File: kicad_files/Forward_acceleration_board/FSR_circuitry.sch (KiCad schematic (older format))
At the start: 49 parts

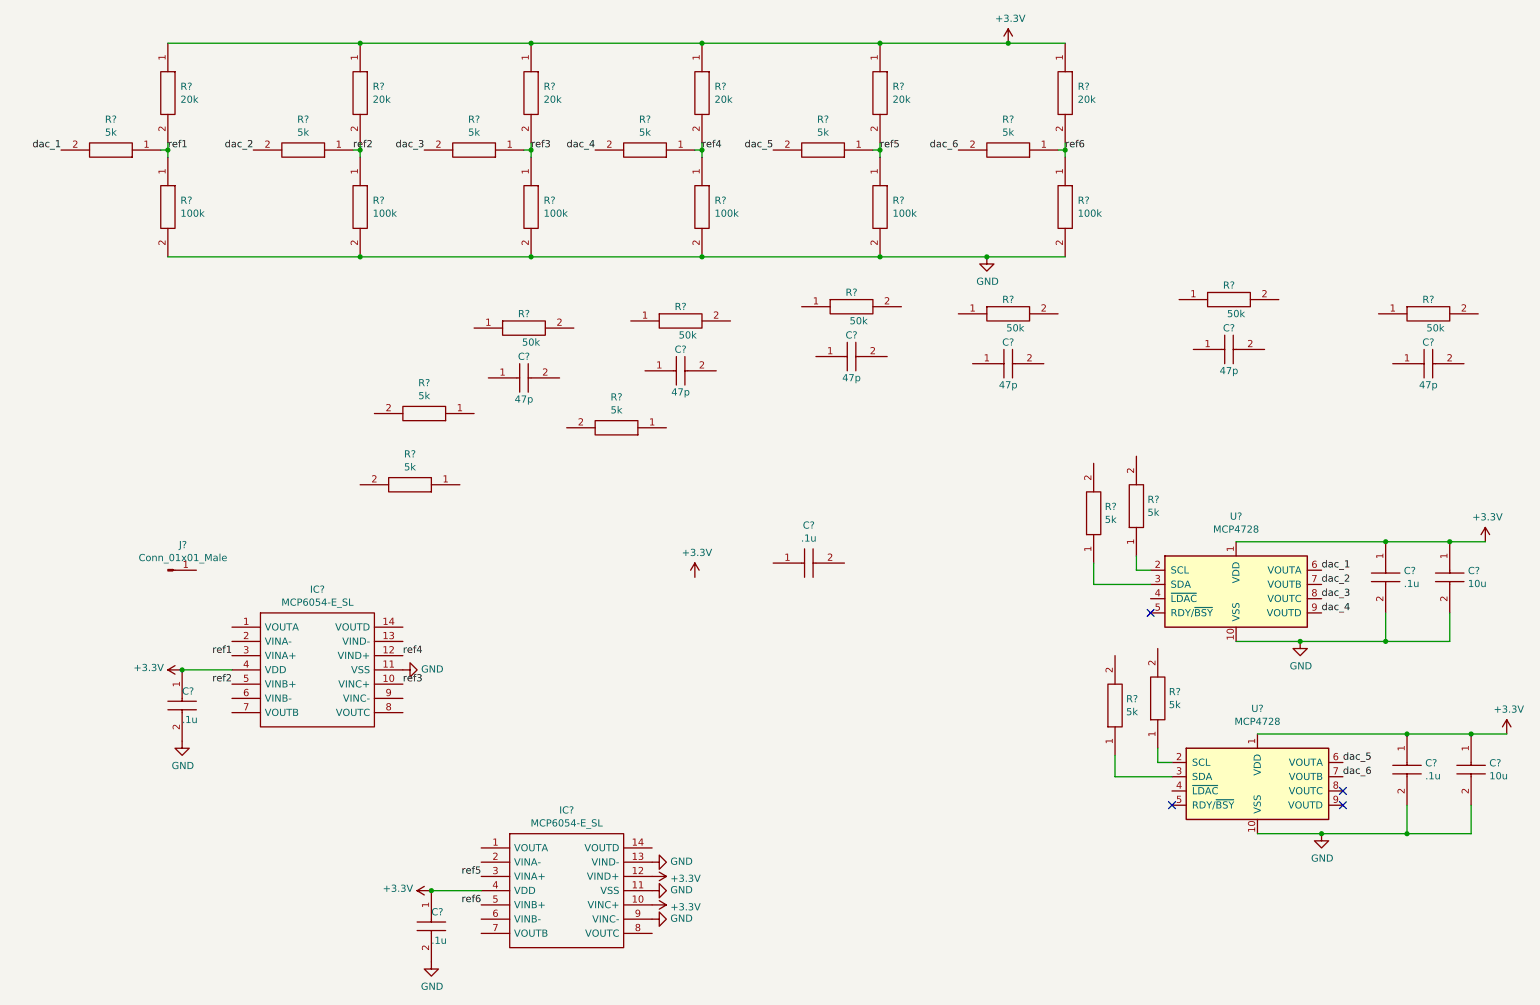
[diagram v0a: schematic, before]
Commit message: reogranized file locations, improved DSC controller pcb with edged margin on edges and rounded corners.  Completed Acceleration control board schematic
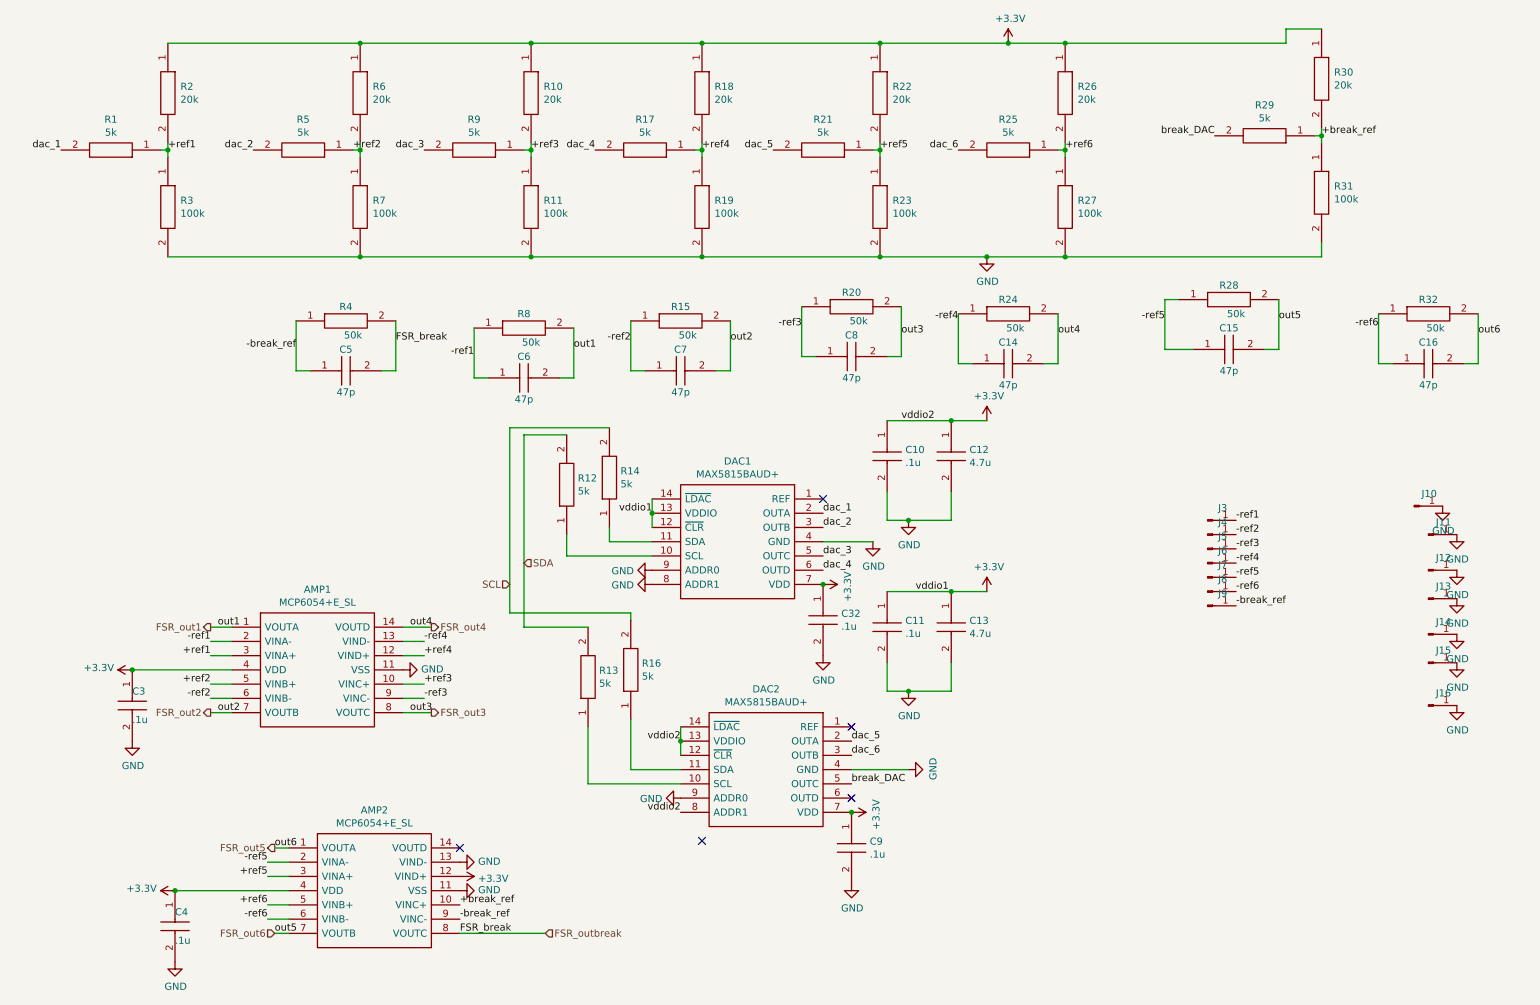
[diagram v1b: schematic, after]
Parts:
- removed C? (x2): .1u, CAPC2012X145N, symbol AS0805KKX7R0BB104:AS0805KKX7R0BB104
- removed C? (x2): 10u, CAPC1005X55N, symbol GRM155C80G106ME44D:GRM155C80G106ME44D
- removed J?: Conn_01x01_Male, symbol Connector:Conn_01x01_Male
- removed R? (x3): 5k, RESC1608X55N, symbol MCT0603PD4991DP500:MCT0603PD4991DP500
- removed U? (x2): MCP4728, Package_SO:MSOP-10_3x3mm_P0.5mm, symbol Analog_DAC:MCP4728
- added C10, C32, C9: .1u, AS0805KKX7R0BB104:CAPC2012X145N, symbol AS0805KKX7R0BB104:AS0805KKX7R0BB104
- added C12, C13: 4.7u, CGA6M3X7S2A475K200AB:CAPC3225X200N, symbol CGA6M3X7S2A475K200AB:CGA6M3X7S2A475K200AB
- added C5: 47p, GRM155C91C105ME11J:CAPC1005X55N, symbol GRM1555C1H470FA01J:GRM1555C1H470FA01J
- added DAC1, DAC2: MAX5815BAUD+, MAX5815BAUD+:SOP65P640X110-14N, symbol MAX5815BAUD+:MAX5815BAUD+
- added J10, J11, J12, J13, J14, J15, J16, J3, J4, J5, J6, J7, J8, J9: Conn_01x01_Male, symbol Connector:Conn_01x01_Male
- added R29: 5k, ERJ3RQF4R7V:RESC1608X55N, symbol MCT0603PD4991DP500:MCT0603PD4991DP500
- added R30: 20k, ERJ3RQF4R7V:RESC1608X55N, symbol MCT0603PD2002DP500:MCT0603PD2002DP500
- added R31: 100k, ERJ3RQF4R7V:RESC1608X55N, symbol MCT0603PD1003DP500:MCT0603PD1003DP500
- added R4: 50k, ERJ3RQF4R7V:RESC1608X55N, symbol MCT0603PD4992DP500:MCT0603PD4992DP500
- AMP1, AMP2: renamed from IC?; value MCP6054-E_SL -> MCP6054+E_SL; footprint SOIC127P600X175-14N -> MCP6054-E_SL:SOIC127P600X175-14N
- C11, C3, C4: renamed from C?; footprint CAPC2012X145N -> AS0805KKX7R0BB104:CAPC2012X145N
- C14, C15, C16, C6, C7, C8: renamed from C?; footprint CAPC1005X55N -> GRM155C91C105ME11J:CAPC1005X55N
- R1, R10, R11, R12, R13, R14, R15, R16, R17, R18, R19, R2, R20, R21, R22, R23, R24, R25, R26, R27, R28, R3, R32, R5, R6, R7, R8, R9: renamed from R?; footprint RESC1608X55N -> ERJ3RQF4R7V:RESC1608X55N
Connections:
- net +3V3: now also C10.1, C12.1, C13.1, C32.1, C9.1, DAC1.12 (~CLR), DAC1.13 (VDDIO), DAC1.14 (~LDAC), DAC1.7 (VDD), DAC2.12 (~CLR), DAC2.13 (VDDIO), DAC2.14 (~LDAC), DAC2.7 (VDD), DAC2.8 (ADDR1), R30.1; no longer AMP2.10 (VINC+)
- net GND: now also C10.2, C12.2, C13.2, C32.2, C9.2, DAC1.4 (GND), DAC1.8 (ADDR1), DAC1.9 (ADDR0), DAC2.4 (GND), DAC2.9 (ADDR0), J10.1 (Pin_1), J11.1 (Pin_1), J12.1 (Pin_1), J13.1 (Pin_1), J14.1 (Pin_1), J15.1 (Pin_1), J16.1 (Pin_1), R31.2; no longer AMP2.9 (VINC-)
- net dac_1: now also DAC1.2 (OUTA)
- net dac_2: now also DAC1.3 (OUTB)
- net dac_3: now also DAC1.5 (OUTC)
- net dac_4: now also DAC1.6 (OUTD)
- net dac_5: now also DAC2.2 (OUTA)
- net dac_6: now also DAC2.3 (OUTB)
- net -ref1: now reaches R8.1
- net -ref1: now also AMP1.2 (VINA-), C6.1, J3.1 (Pin_1)
- net FSR_out1: now reaches R8.2
- net FSR_out1: now also AMP1.1 (VOUTA), C6.2
- net at R16.1: now also DAC2.11 (SDA)
- net at R13.1: now also DAC2.10 (SCL)
- net FSR_out5: now reaches AMP2.1 (VOUTA)
- net FSR_out5: now also C16.2, R32.2
- net -ref5: now reaches AMP2.2 (VINA-)
- net -ref5: now also C15.1, R28.1, J7.1 (Pin_1)
- net -ref6: now reaches AMP2.6 (VINB-)
- net -ref6: now also C16.1, R32.1, J8.1 (Pin_1)
- net FSR_out6: now reaches AMP2.7 (VOUTB)
- net FSR_out6: now also C15.2, R28.2
- net FSR_outbreak: now reaches AMP2.8 (VOUTC)
- net FSR_outbreak: now also C5.2, R4.2
- net -ref4: now reaches AMP1.13 (VIND-)
- net -ref4: now also C14.1, R24.1, J6.1 (Pin_1)
- net FSR_out4: now reaches AMP1.14 (VOUTD)
- net FSR_out4: now also C14.2, R24.2
- net -ref2: now reaches AMP1.6 (VINB-)
- net -ref2: now also C7.1, R15.1, J4.1 (Pin_1)
- net FSR_out2: now reaches AMP1.7 (VOUTB)
- net FSR_out2: now also C7.2, R15.2
- net FSR_out3: now reaches AMP1.8 (VOUTC)
- net FSR_out3: now also C8.2, R20.2
- net -ref3: now reaches AMP1.9 (VINC-)
- net -ref3: now also C8.1, R20.1, J5.1 (Pin_1)
- net SDA: now reaches R13.2
- net SDA: now also R12.2
- net SCL: now reaches R16.2
- net SCL: now also R14.2
- net at R14.1: now also DAC1.11 (SDA)
- net at R12.1: now also DAC1.10 (SCL)
- net ref1 renamed +ref1
- net ref2 renamed +ref2
- net ref3 renamed +ref3
- net ref4 renamed +ref4
- net ref5 renamed +ref5
- net ref6 renamed +ref6
- new net +break_ref: AMP2.10 (VINC+), R29.1, R30.2, R31.1
- new net -break_ref: AMP2.9 (VINC-), C5.1, J9.1 (Pin_1), R4.1
- new net break_DAC: DAC2.5 (OUTC), R29.2
- no-connect marks 4 -> 5
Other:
- moved on the sheet: AMP2, C11, C3, C4, R12, R13, R14, R16

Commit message: nearly completed forward acceleration control board rounded edges and established clearence for motor control board made progress canabalizing Vedder's code for motor control
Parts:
- J10, J11, J12, J13, J14, J15, J16, J3, J4, J5, J6, J7, J8, J9: footprint (none) -> Wire_Pads:SolderWirePad_1x01_SMD_1.27x2.54mm
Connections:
- net +3V3: now also AMP1.12 (VIND+), R29.2; no longer AMP2.12 (VIND+), R30.1
- net +break_ref: now also R17.2, R18.2, R19.1; no longer R29.1, R30.2, R31.1
- net +ref1: now also R1.2; no longer R1.1
- net +ref2: now also R5.2; no longer R5.1
- net +ref3: now also R9.2; no longer R9.1
- net +ref4: now also AMP2.12 (VIND+), R29.1, R30.1, R31.1; no longer AMP1.12 (VIND+), R17.1, R18.2, R19.1
- net +ref5: now also R21.2; no longer R21.1
- net +ref6: now also R25.2; no longer R25.1
- net -break_ref: now also C14.1, R24.1; no longer C5.1, R4.1
- net -ref4: now also AMP2.13 (VIND-), C5.1, R4.1; no longer AMP1.13 (VIND-), C14.1, R24.1
- net FSR_out4: now also AMP2.14 (VOUTD), C5.2, R4.2; no longer AMP1.14 (VOUTD), C14.2, R24.2
- net FSR_out5: now also C15.2, R28.2; no longer C16.2, R32.2
- net FSR_out6: now also C16.2, R32.2; no longer C15.2, R28.2
- net FSR_outbreak: now also C14.2, R24.2; no longer C5.2, R4.2
- net GND: now also AMP1.13 (VIND-); no longer AMP2.13 (VIND-)
- net break_DAC: now also R17.1; no longer R29.2
- net dac_1: now also R1.1; no longer R1.2
- net dac_2: now also R5.1; no longer R5.2
- net dac_3: now also R9.1; no longer R9.2
- net dac_4: now also DAC2.6 (OUTD), R30.2; no longer DAC1.6 (OUTD), R17.2
- net dac_5: now also R21.1; no longer R21.2
- net dac_6: now also R25.1; no longer R25.2
- no-connect marks 5 -> 4
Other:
- moved on the sheet: C14, R17, R18, R19, R21, R22, R23, R24, R25, R26, R27, R29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

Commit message: updated BOMS for boards and added battery pack wiring schematic
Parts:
- J10, J11, J12, J13, J14, J15, J16, J3, J4, J5, J6, J7, J8, J9: symbol Connector:Conn_01x01_Male -> Forward_acceleration_board-rescue:Conn_01x01_Male-Connector
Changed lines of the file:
@@
 $EndComp
 $Comp
-L power:GND #PWR0105
+L Forward_acceleration_board-rescue:GND-power #PWR0105
 U 1 1 5D8E34E0
 P 3200 5200
@@
 Connection ~ 4100 800
 $Comp
-L power:+3.3V #PWR0107
+L Forward_acceleration_board-rescue:+3.3V-power #PWR0107
 U 1 1 5D8E6EA9
 P 7450 800
@@
 Connection ~ 4100 2300
 $Comp
-L power:GND #PWR0108
+L Forward_acceleration_board-rescue:GND-power #PWR0108
 U 1 1 5D8EB31F
 P 7300 2300
@@
 $EndComp
 $Comp
-L power:+3.3V #PWR0109
+L Forward_acceleration_board-rescue:+3.3V-power #PWR0109
 U 1 1 5D8E337A
 P 1600 6750
@@
 Connection ~ 1600 6750
 $Comp
-L power:GND #PWR0110
+L Forward_acceleration_board-rescue:GND-power #PWR0110
 U 1 1 5D8F17E9
 P 1600 7250
@@
 $EndComp
 $Comp
-L power:+3.3V #PWR0111
+L Forward_acceleration_board-rescue:+3.3V-power #PWR0111
 U 1 1 5D8F1D89
 P 1300 5200
@@
 	2000 5200 1300 5200
 $Comp
-L power:GND #PWR0112
+L Forward_acceleration_board-rescue:GND-power #PWR0112
 U 1 1 5D8F1D91
 P 1300 5700
@@
 $EndComp
 $Comp
-L power:+3.3V #PWR0113
+L Forward_acceleration_board-rescue:+3.3V-power #PWR0113
 U 1 1 5D908625
 P 7300 4650
@@
 	6600 5150 6600 5350
 $Comp
-L power:GND #PWR0114
+L Forward_acceleration_board-rescue:GND-power #PWR0114
 U 1 1 5D908644
 P 6500 4300
@@
 break_DAC
 $Comp
-L Connector:Conn_01x01_Male J3
+L Forward_acceleration_board-rescue:Conn_01x01_Male-Connector J3
 U 1 1 5D9E5847
 P 8850 4150
+AR Path="/5D9E5847" Ref="J3"  Part="1"
+AR Path="/5D8CBEA0/5D9E5847" Ref="J3"  Part="1"
 F 0 "J3" H 8956 4237 50  0000 C CNN
 F 1 "Conn_01x01_Male" H 8956 4237 50  0001 C CNN
@@
 $EndComp
 $Comp
-L Connector:Conn_01x01_Male J4
+L Forward_acceleration_board-rescue:Conn_01x01_Male-Connector J4
 U 1 1 5D9E58E5
 P 8850 4250
+AR Path="/5D9E58E5" Ref="J4"  Part="1"
+AR Path="/5D8CBEA0/5D9E58E5" Ref="J4"  Part="1"
 F 0 "J4" H 8956 4337 50  0000 C CNN
 F 1 "Conn_01x01_Male" H 8956 4337 50  0001 C CNN
@@
 $EndComp
 $Comp
-L Connector:Conn_01x01_Male J6
+L Forward_acceleration_board-rescue:Conn_01x01_Male-Connector J6
 U 1 1 5D9E59AA
 P 8850 4450
+AR Path="/5D9E59AA" Ref="J6"  Part="1"
+AR Path="/5D8CBEA0/5D9E59AA" Ref="J6"  Part="1"
 F 0 "J6" H 8956 4537 50  0000 C CNN
 F 1 "Conn_01x01_Male" H 8956 4537 50  0001 C CNN
@@
 $EndComp
 $Comp
-L Connector:Conn_01x01_Male J5
+L Forward_acceleration_board-rescue:Conn_01x01_Male-Connector J5
 U 1 1 5D9E5A72
 P 8850 4350
+AR Path="/5D9E5A72" Ref="J5"  Part="1"
+AR Path="/5D8CBEA0/5D9E5A72" Ref="J5"  Part="1"
 F 0 "J5" H 8956 4437 50  0000 C CNN
 F 1 "Conn_01x01_Male" H 8956 4437 50  0001 C CNN
@@
 $EndComp
 $Comp
-L Connector:Conn_01x01_Male J7
+L Forward_acceleration_board-rescue:Conn_01x01_Male-Connector J7
 U 1 1 5D9E5CB8
 P 8850 4550
+AR Path="/5D9E5CB8" Ref="J7"  Part="1"
+AR Path="/5D8CBEA0/5D9E5CB8" Ref="J7"  Part="1"
 F 0 "J7" H 8956 4637 50  0000 C CNN
 F 1 "Conn_01x01_Male" H 8956 4637 50  0001 C CNN
@@
 $EndComp
 $Comp
-L Connector:Conn_01x01_Male J8
+L Forward_acceleration_board-rescue:Conn_01x01_Male-Connector J8
 U 1 1 5D9E5D3A
 P 8850 4650
+AR Path="/5D9E5D3A" Ref="J8"  Part="1"
+AR Path="/5D8CBEA0/5D9E5D3A" Ref="J8"  Part="1"
 F 0 "J8" H 8956 4737 50  0000 C CNN
 F 1 "Conn_01x01_Male" H 8956 4737 50  0001 C CNN
@@
 $EndComp
 $Comp
-L Connector:Conn_01x01_Male J9
+L Forward_acceleration_board-rescue:Conn_01x01_Male-Connector J9
 U 1 1 5D9E5DC8
 P 8850 4750
+AR Path="/5D9E5DC8" Ref="J9"  Part="1"
+AR Path="/5D8CBEA0/5D9E5DC8" Ref="J9"  Part="1"
 F 0 "J9" H 8956 4837 50  0000 C CNN
 F 1 "Conn_01x01_Male" H 8956 4837 50  0001 C CNN
@@
 $EndComp
 $Comp
-L Connector:Conn_01x01_Male J10
+L Forward_acceleration_board-rescue:Conn_01x01_Male-Connector J10
 U 1 1 5D9E5F6F
 P 10300 4050
+AR Path="/5D9E5F6F" Ref="J10"  Part="1"
+AR Path="/5D8CBEA0/5D9E5F6F" Ref="J10"  Part="1"
 F 0 "J10" H 10406 4137 50  0000 C CNN
 F 1 "Conn_01x01_Male" H 10406 4137 50  0001 C CNN
@@
 $EndComp
 $Comp
-L Connector:Conn_01x01_Male J11
+L Forward_acceleration_board-rescue:Conn_01x01_Male-Connector J11
 U 1 1 5D9E5F76
 P 10400 4250
+AR Path="/5D9E5F76" Ref="J11"  Part="1"
+AR Path="/5D8CBEA0/5D9E5F76" Ref="J11"  Part="1"
 F 0 "J11" H 10506 4337 50  0000 C CNN
 F 1 "Conn_01x01_Male" H 10506 4337 50  0001 C CNN
@@
 $EndComp
 $Comp
-L Connector:Conn_01x01_Male J12
+L Forward_acceleration_board-rescue:Conn_01x01_Male-Connector J12
 U 1 1 5D9E5F7D
 P 10400 4500
+AR Path="/5D9E5F7D" Ref="J12"  Part="1"
+AR Path="/5D8CBEA0/5D9E5F7D" Ref="J12"  Part="1"
 F 0 "J12" H 10506 4587 50  0000 C CNN
 F 1 "Conn_01x01_Male" H 10506 4587 50  0001 C CNN
@@
 $EndComp
 $Comp
-L Connector:Conn_01x01_Male J13
+L Forward_acceleration_board-rescue:Conn_01x01_Male-Connector J13
 U 1 1 5D9E5F84
 P 10400 4700
+AR Path="/5D9E5F84" Ref="J13"  Part="1"
+AR Path="/5D8CBEA0/5D9E5F84" Ref="J13"  Part="1"
 F 0 "J13" H 10506 4787 50  0000 C CNN
 F 1 "Conn_01x01_Male" H 10506 4787 50  0001 C CNN
@@
 $EndComp
 $Comp
-L Connector:Conn_01x01_Male J14
+L Forward_acceleration_board-rescue:Conn_01x01_Male-Connector J14
 U 1 1 5D9E5F8B
 P 10400 4950
+AR Path="/5D9E5F8B" Ref="J14"  Part="1"
+AR Path="/5D8CBEA0/5D9E5F8B" Ref="J14"  Part="1"
 F 0 "J14" H 10506 5037 50  0000 C CNN
 F 1 "Conn_01x01_Male" H 10506 5037 50  0001 C CNN
@@
 $EndComp
 $Comp
-L Connector:Conn_01x01_Male J15
+L Forward_acceleration_board-rescue:Conn_01x01_Male-Connector J15
 U 1 1 5D9E5F92
 P 10400 5150
+AR Path="/5D9E5F92" Ref="J15"  Part="1"
+AR Path="/5D8CBEA0/5D9E5F92" Ref="J15"  Part="1"
 F 0 "J15" H 10506 5237 50  0000 C CNN
 F 1 "Conn_01x01_Male" H 10506 5237 50  0001 C CNN
@@
 $EndComp
 $Comp
-L Connector:Conn_01x01_Male J16
+L Forward_acceleration_board-rescue:Conn_01x01_Male-Connector J16
 U 1 1 5D9E5F99
 P 10400 5450
+AR Path="/5D9E5F99" Ref="J16"  Part="1"
+AR Path="/5D8CBEA0/5D9E5F99" Ref="J16"  Part="1"
 F 0 "J16" H 10506 5537 50  0000 C CNN
 F 1 "Conn_01x01_Male" H 10506 5537 50  0001 C CNN
@@
 $EndComp
 $Comp
-L power:GND #PWR0117
+L Forward_acceleration_board-rescue:GND-power #PWR0117
 U 1 1 5D9EA9F2
 P 10600 4950
@@
 $EndComp
 $Comp
-L power:GND #PWR0118
+L Forward_acceleration_board-rescue:GND-power #PWR0118
 U 1 1 5D9EAFE2
 P 10500 4050
@@
 $EndComp
 $Comp
-L power:GND #PWR0119
+L Forward_acceleration_board-rescue:GND-power #PWR0119
 U 1 1 5D9EB06B
 P 10600 4250
@@
 $EndComp
 $Comp
-L power:GND #PWR0120
+L Forward_acceleration_board-rescue:GND-power #PWR0120
 U 1 1 5D9EB133
 P 10600 4500
@@
 $EndComp
 $Comp
-L power:GND #PWR0121
+L Forward_acceleration_board-rescue:GND-power #PWR0121
 U 1 1 5D9EB3BE
 P 10600 4700
@@
 $EndComp
 $Comp
-L power:GND #PWR0122
+L Forward_acceleration_board-rescue:GND-power #PWR0122
 U 1 1 5D9EBD62
 P 10600 5150
@@
 $EndComp
 $Comp
-L power:GND #PWR0125
+L Forward_acceleration_board-rescue:GND-power #PWR0125
 U 1 1 5D9EBEB2
 P 10600 5450
@@
 	6600 5350 6750 5350
 $Comp
-L power:GND #PWR0126
+L Forward_acceleration_board-rescue:GND-power #PWR0126
 U 1 1 5DA2AB93
 P 6750 5350
@@
 	6750 5350 7050 5350
 $Comp
-L power:+3.3V #PWR0127
+L Forward_acceleration_board-rescue:+3.3V-power #PWR0127
 U 1 1 5DA3C029
 P 7300 3450
@@
 	6600 4150 6750 4150
 $Comp
-L power:GND #PWR0128
+L Forward_acceleration_board-rescue:GND-power #PWR0128
 U 1 1 5DA3C051
 P 6750 4150
@@
 	6750 4150 7050 4150
 $Comp
-L power:GND #PWR0129
+L Forward_acceleration_board-rescue:GND-power #PWR0129
 U 1 1 5DA4BB6C
 P 5150 6100
@@
 vddio2
 $Comp
-L power:GND #PWR0130
+L Forward_acceleration_board-rescue:GND-power #PWR0130
 U 1 1 5DA6DB6A
 P 4950 4500
@@
 $EndComp
 $Comp
-L power:GND #PWR0131
+L Forward_acceleration_board-rescue:GND-power #PWR0131
 U 1 1 5DA6DC32
 P 4950 4600
@@
 Connection ~ 4950 4100
 $Comp
-L power:+3.3V #PWR0132
+L Forward_acceleration_board-rescue:+3.3V-power #PWR0132
 U 1 1 5DA881D7
 P 6350 6200
@@
 $EndComp
 $Comp
-L power:GND #PWR0133
+L Forward_acceleration_board-rescue:GND-power #PWR0133
 U 1 1 5DA9B845
 P 6350 6700
@@
 Connection ~ 6350 6200
 $Comp
-L power:GND #PWR0134
+L Forward_acceleration_board-rescue:GND-power #PWR0134
 U 1 1 5DAD0812
 P 6750 5900
@@
 NoConn ~ 5300 6400
 $Comp
-L power:+3.3V #PWR0158
+L Forward_acceleration_board-rescue:+3.3V-power #PWR0158
 U 1 1 5D9D7BCD
 P 6150 4600
@@
 $EndComp
 $Comp
-L power:GND #PWR0159
+L Forward_acceleration_board-rescue:GND-power #PWR0159
 U 1 1 5D9D7BE1
 P 6150 5100
@@
 NoConn ~ 3200 4900
 $Comp
-L power:+3.3V #PWR0115
+L Forward_acceleration_board-rescue:+3.3V-power #PWR0115
 U 1 1 5D8E3118
 P 3350 5100
@@
 $EndComp
 $Comp
-L power:GND #PWR0116
+L Forward_acceleration_board-rescue:GND-power #PWR0116
 U 1 1 5D8E22C7
 P 3350 5000
@@
 $EndComp
 $Comp
-L power:GND #PWR0106
+L Forward_acceleration_board-rescue:GND-power #PWR0106
 U 1 1 5D8E353F
 P 3600 6750
